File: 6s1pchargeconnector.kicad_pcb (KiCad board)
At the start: 2 copper layers, 8 parts, among them P1 CONN_01X07, P2 CONN_01X02, P3 CONN_01X02, P4 CONN_01X02, P5 CONN_01X02, P6 CONN_01X02, P7 CONN_01X02, P8 CONN_01X02

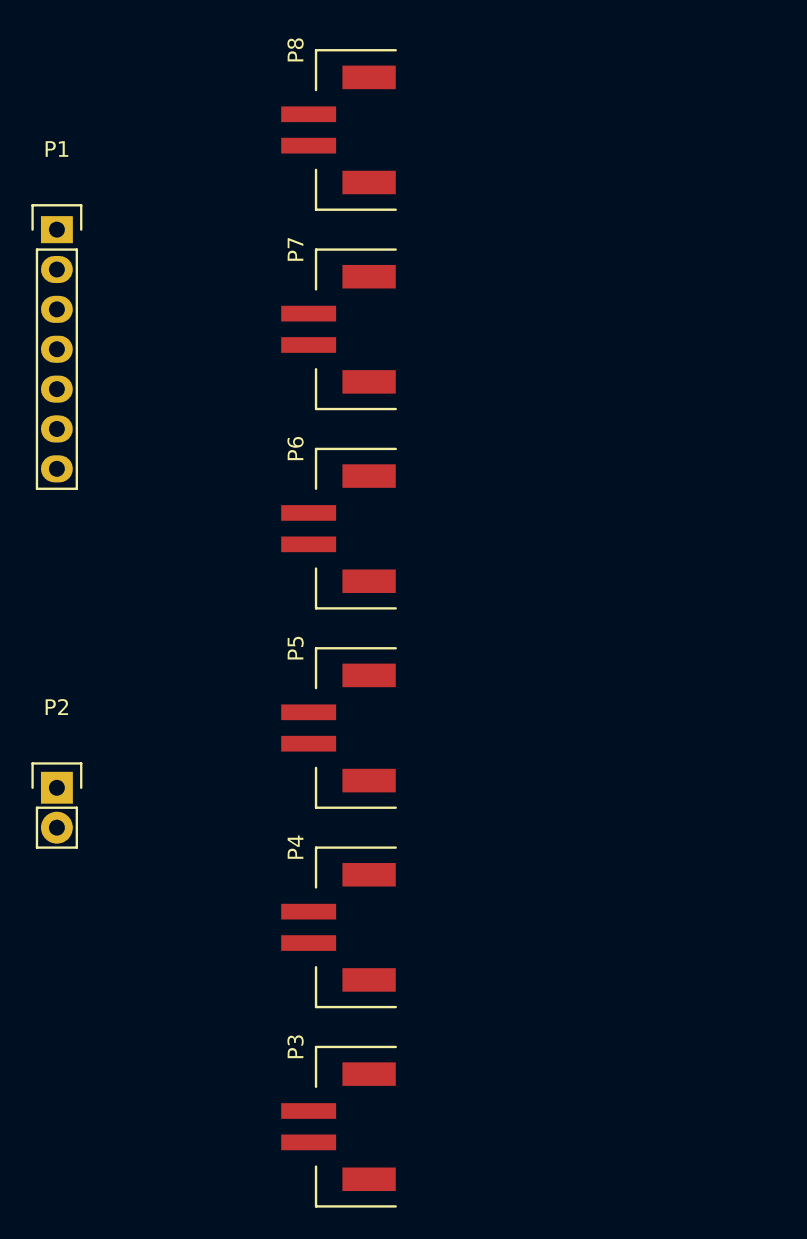
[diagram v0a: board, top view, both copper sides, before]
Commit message: Added the other two connectors, pcb, gerbers, and bom.
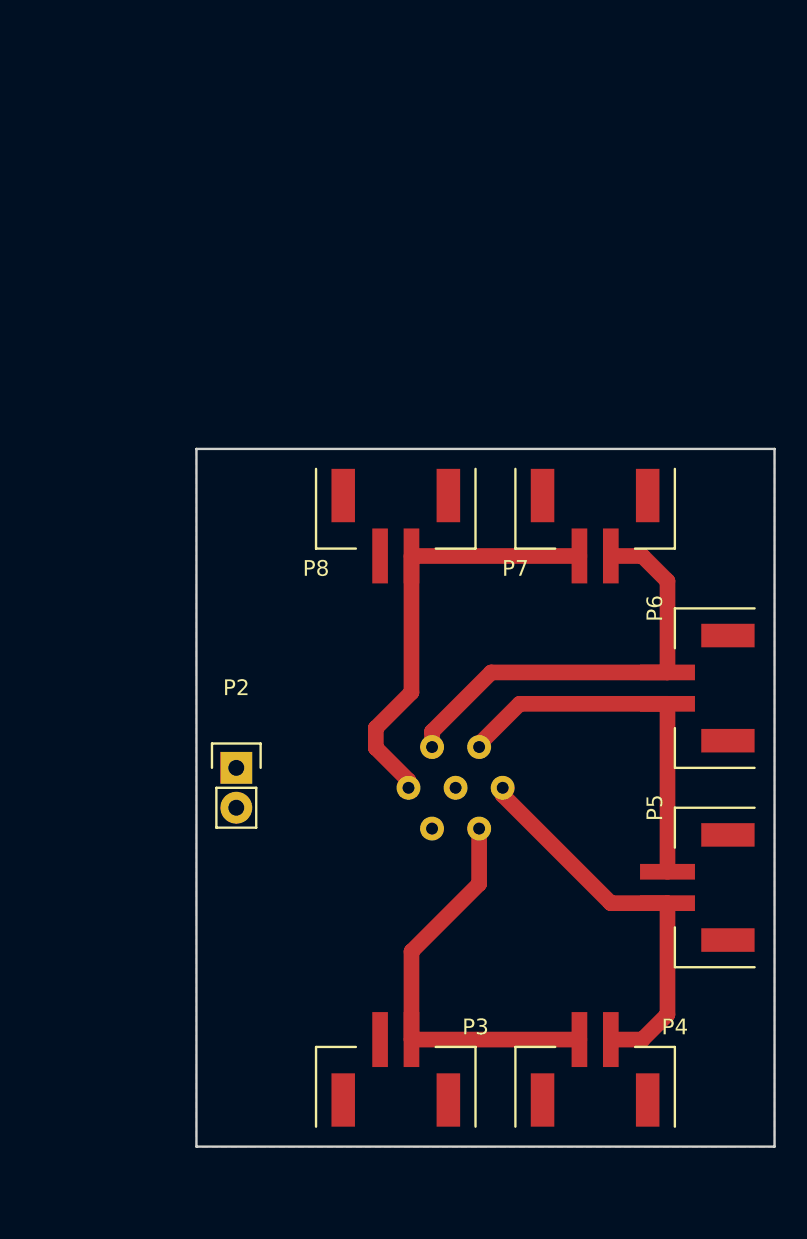
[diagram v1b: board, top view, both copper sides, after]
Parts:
- P1: value CONN_01X07 -> CHARGE; footprint Pin_Headers:Pin_Header_Straight_1x07 -> Connectors LEMO:ECG.0B.307; moved to B.Cu
- P2: value CONN_01X02 -> OUT
- P3: value CONN_01X02 -> BATT 6
- P4: value CONN_01X02 -> BATT 5
- P5: value CONN_01X02 -> BATT 4
- P6: value CONN_01X02 -> BATT 3
- P7: value CONN_01X02 -> BATT 2
- P8: value CONN_01X02 -> BATT 1
- moved P1 43.7 mm to (147.3, 130.8), turned to 180 degrees
- moved P5 25.0 mm to (166.4, 137.2)
- moved P6 25.0 mm to (166.4, 124.5)
- moved P8 21.6 mm to (143.5, 110.5), turned to 180 degrees
- moved P4 18.0 mm to (156.2, 152.4), turned to 0 degrees
- moved P7 15.5 mm to (156.2, 110.5), turned to 180 degrees
- moved P2 11.5 mm to (133.3, 129.5)
- turned P3 to 0 degrees
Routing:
- net Net-(P1-Pad3): track 0.00 -> 27.6 mm
- net Net-(P1-Pad2): track 0.00 -> 27.3 mm
- net Net-(P1-Pad6): track 0.00 -> 25.9 mm
- net Net-(P1-Pad5): track 0.00 -> 25.2 mm
- net Net-(P1-Pad4): track 0.00 -> 23.9 mm
- added copper zone on B.Cu, net Net-(P1-Pad1)
- added copper zone on F.Cu, net Net-(P1-Pad7)
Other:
- board outline added: 36.8 x 44.4 mm
- net class Power added: clearance 0.2, trace_width 1, via_dia 0.6, via_drill 0.4
- rule trace_min: 0.2 -> 0.1524
- rule via_min_drill: 0.3 -> 0.3302
- rule via_min_size: 0.4 -> 0.508
- board text added: "+"
- board text added: "-"

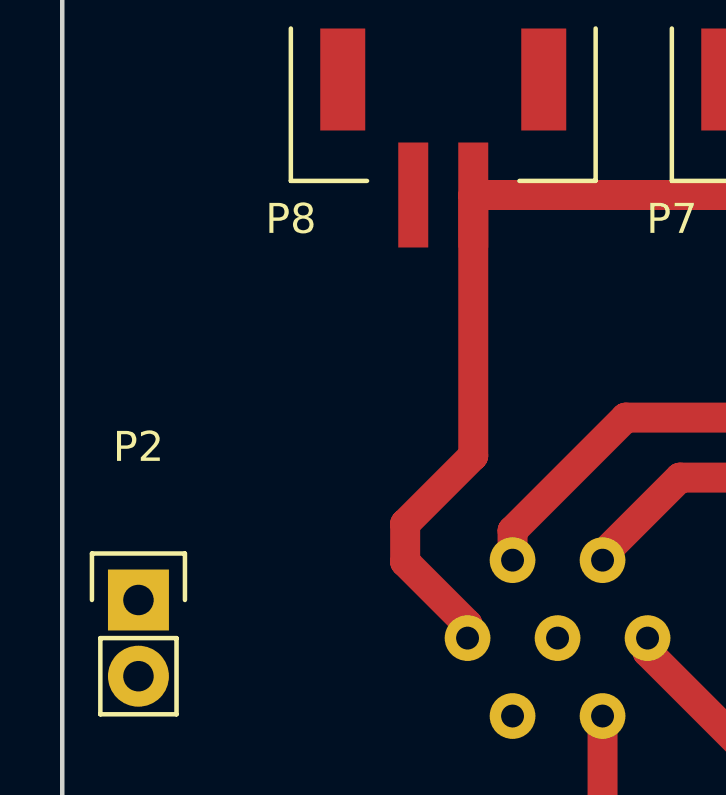
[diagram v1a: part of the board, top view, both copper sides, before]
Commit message: Added a missing trace and updated the gerbers.
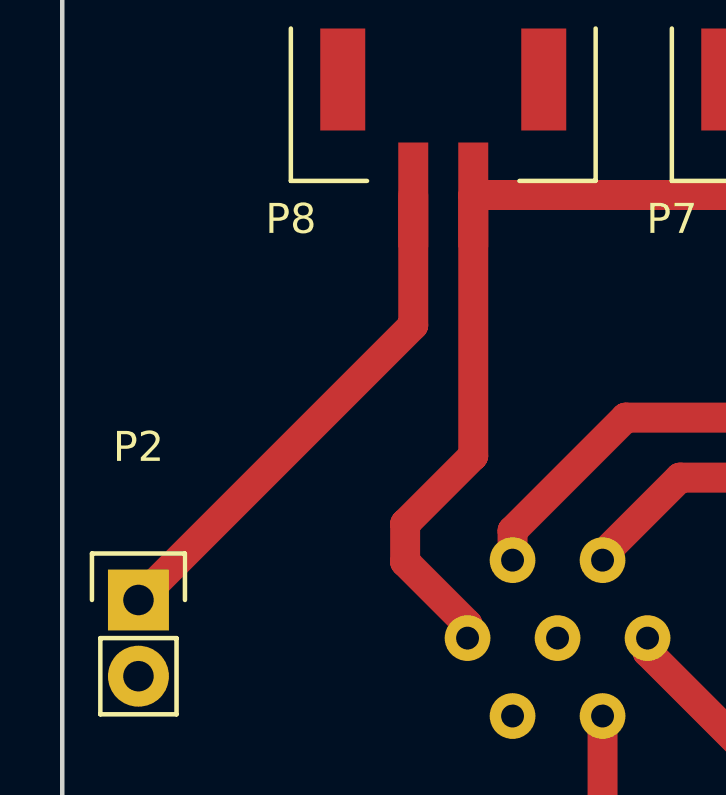
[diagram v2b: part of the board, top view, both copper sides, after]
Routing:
- net Net-(P1-Pad1): track 0.00 -> 17.3 mm
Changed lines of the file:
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@@
   (general
     (links 14)
-    (no_connects 1)
+    (no_connects 0)
     (area 111.380001 96.21 168.615 154.645)
     (thickness 1.6)
     (drawings 9)
-    (tracks 26)
+    (tracks 28)
     (zones 0)
     (modules 8)
@@
   (gr_line (start 167.64 109.22) (end 130.81 109.22) (angle 90) (layer Edge.Cuts) (width 0.15))
   (gr_line (start 167.64 153.67) (end 167.64 109.22) (angle 90) (layer Edge.Cuts) (width 0.15))
+  (segment (start 142.51 116.04) (end 142.51 120.38) (width 1) (layer F.Cu) (net 1))
+  (segment (start 142.51 120.38) (end 133.35 129.54) (width 1) (layer F.Cu) (net 1))
   (segment (start 144.32 130.81) (end 144.32 130.35) (width 1) (layer F.Cu) (net 2))
   (segment (start 144.32 130.35) (end 142.24 128.27) (width 1) (layer F.Cu) (net 2))
